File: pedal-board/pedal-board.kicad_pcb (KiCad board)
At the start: 2 copper layers, 168 x 64 mm, 42 parts, among them J1 AudioJack0, J2 AudioJack1, J3 AudioJack2, J4 AudioJack3, J5 SPI, U1 MCP3004

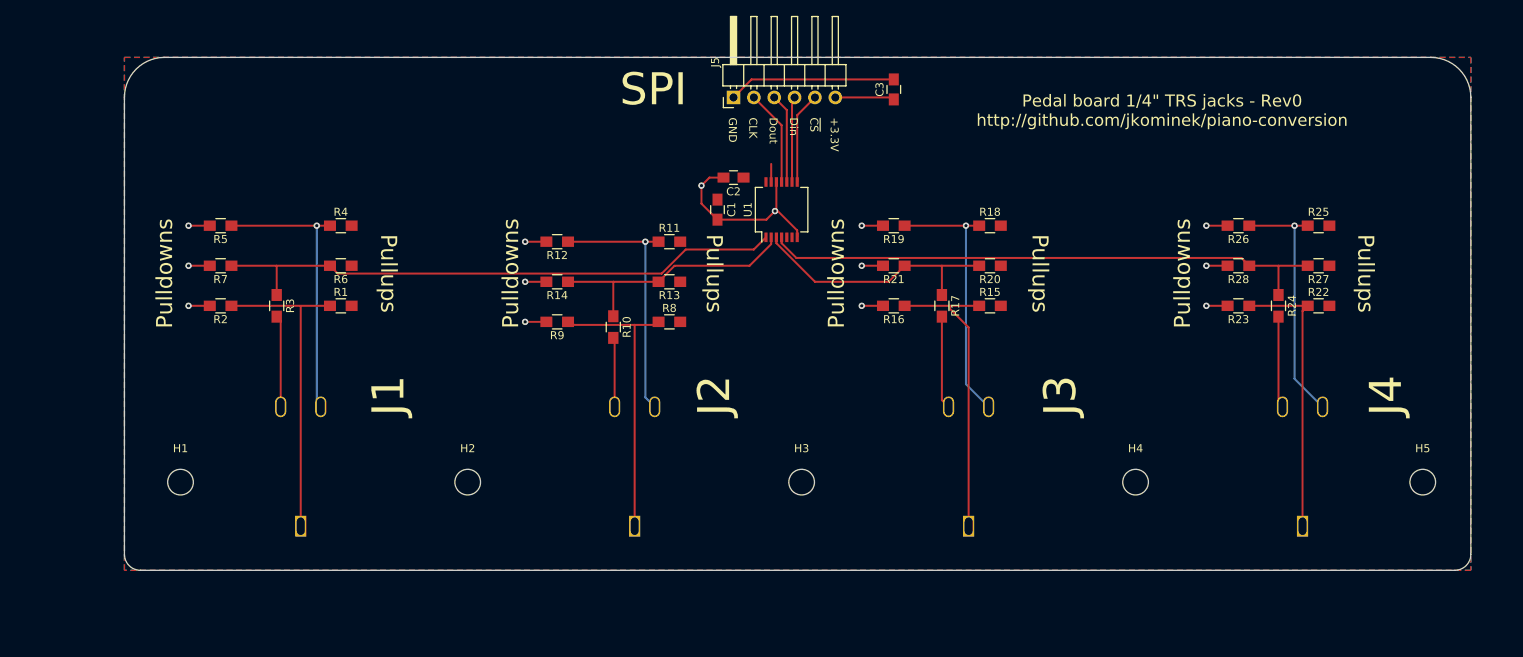
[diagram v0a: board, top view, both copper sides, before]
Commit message: Convert pedal board over to I2C/Qwiic. Adjust mounting hole spacing.
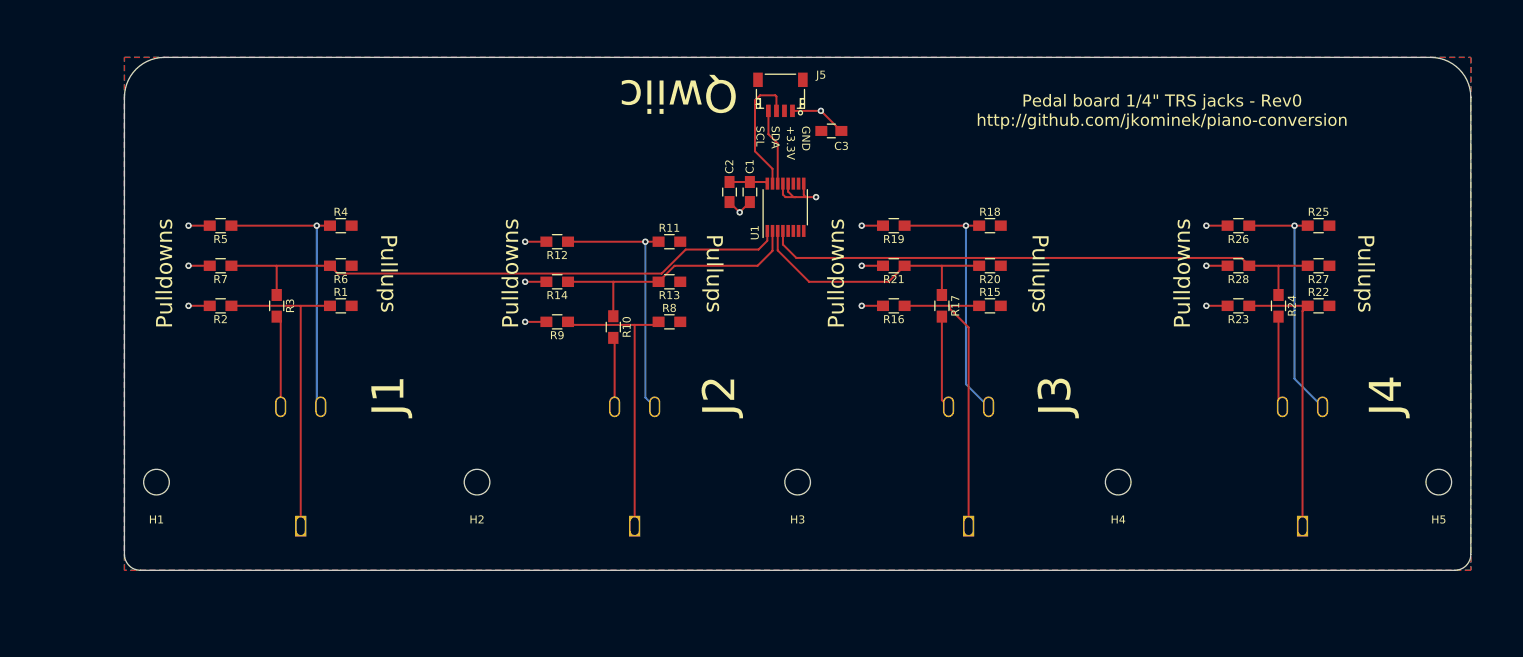
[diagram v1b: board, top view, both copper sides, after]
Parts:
- J5: value SPI -> Qwiic; footprint Pin_Headers:Pin_Header_Angled_1x06_Pitch2.54mm -> Connectors_JST:JST_SH_SM04B-SRSS-TB_04x1.00mm_Angled
- U1: value MCP3004 -> ADS7830; footprint Housings_SSOP:SSOP-14_5.3x6.2mm_Pitch0.65mm -> Housings_SSOP:TSSOP-16_4.4x5mm_Pitch0.65mm
- moved C3 9.36 mm to (116.2, 43.2), turned to 0 degrees
- moved J5 5.86 mm to (109.9, 38.7), turned to 180 degrees
- moved C1 4.60 mm to (106.0, 50.8)
- moved H1 3.00 mm to (32.0, 87.0)
- moved H4 2.17 mm to (152.0, 87.0)
- moved H5 2.00 mm to (192.0, 87.0)
- moved C2 1.87 mm to (103.5, 50.8), turned to 270 degrees
- moved H2 1.17 mm to (72.0, 87.0)
- moved U1 0.57 mm to (110.5, 52.7)
- moved H3 0.50 mm to (112.0, 87.0)
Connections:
- J5 pad 2: Net-(J5-Pad2) -> +3V3
- J5 pad 3: Net-(J5-Pad3) -> /SDA
- J5 pad 4: Net-(J5-Pad4) -> /SCL
- U1 pad 10: Net-(J5-Pad3) -> (no net)
- U1 pad 11: Net-(J5-Pad2) -> (no net)
- U1 pad 13: +3V3 -> GND
- U1 pad 14: +3V3 -> /SCL
- U1 pad 7: GND -> (no net)
- U1 pad 8: Net-(J5-Pad5) -> (no net)
- U1 pad 9: Net-(J5-Pad4) -> GND
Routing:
- net GND: track 76.8 -> 52.2 mm, vias 14 -> 15
- net /SDA: track 0.00 -> 16.1 mm
- net Net-(J5-Pad2): track 12.0 -> 0.00 mm
- net Net-(J5-Pad5): track 11.5 -> 0.00 mm
- net Net-(J5-Pad3): track 11.2 -> 0.00 mm
- net Net-(J5-Pad4): track 10.7 -> 0.00 mm
- net /SCL: track 0.00 -> 9.56 mm
- net +3V3: track 9.65 -> 4.79 mm
- net /CH1: track 32.4 -> 33.9 mm
- net /CH0: track 72.6 -> 73.8 mm
- net /CH2: track 32.5 -> 33.7 mm
- net /CH3: track 71.2 -> 71.9 mm
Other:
- board text added: "Qwiic"
- board text added: "SCL"
- board text added: "SDA"
- board text removed: "CLK"
- board text removed: "Din"
- board text removed: "Dout"
- board text removed: "SPI"
- board text removed: "~CS~"

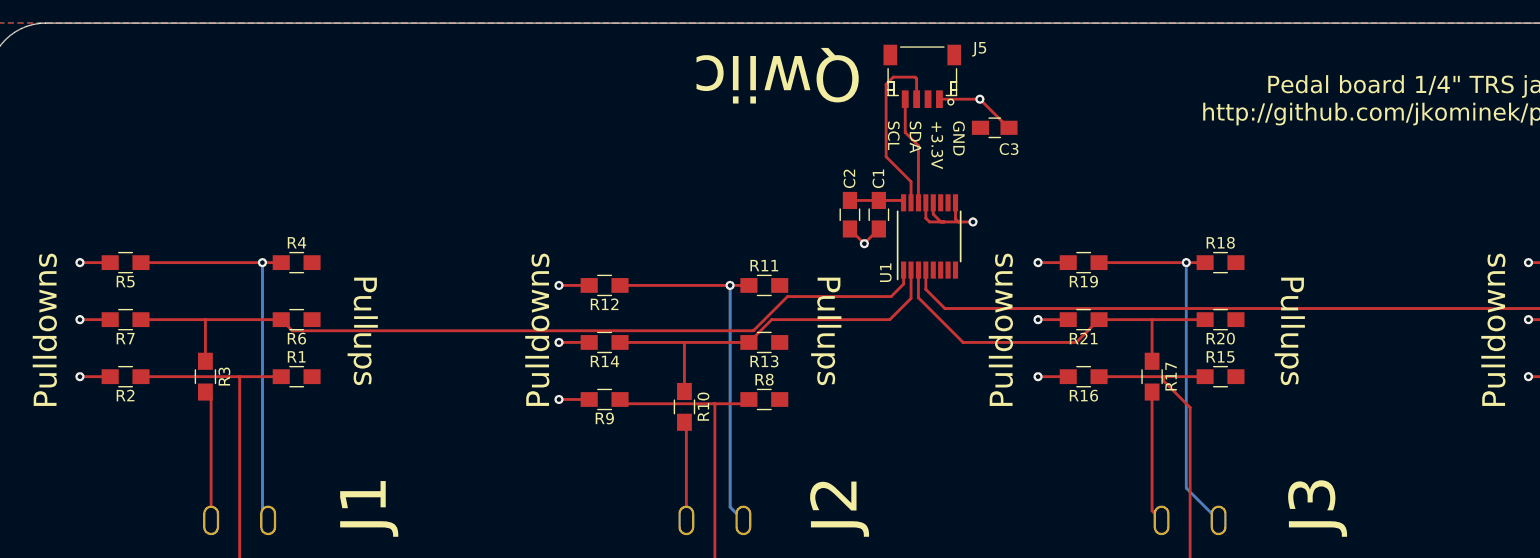
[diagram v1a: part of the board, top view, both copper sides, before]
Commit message: Complete pedal board I2C conversion; make I2C address configurable.
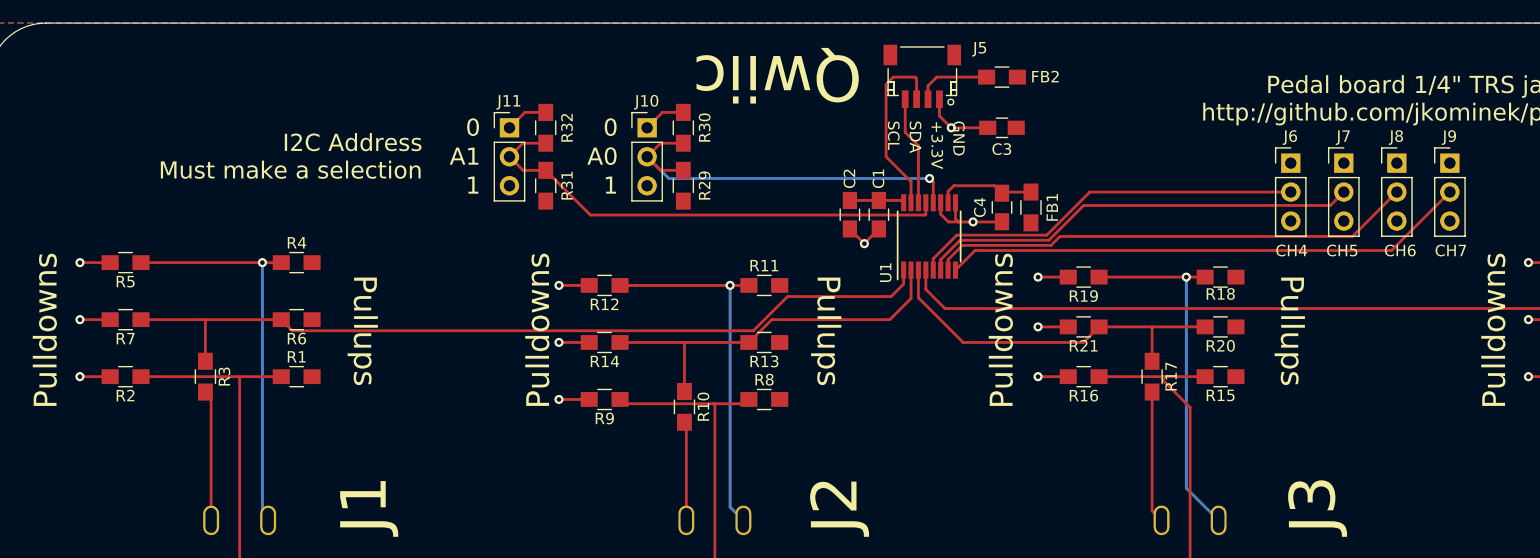
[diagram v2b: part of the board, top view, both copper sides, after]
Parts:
- added C4: 0.1uF, Capacitors_SMD:C_0805_HandSoldering, F.Cu at (116.8, 50.2)
- added FB1: FB, Inductors_SMD:L_0805_HandSoldering, F.Cu at (119.4, 50.2)
- added FB2: FB, Inductors_SMD:L_0805_HandSoldering, F.Cu at (116.8, 38.7)
- added J10: CH7, Pin_Headers:Pin_Header_Straight_1x03_Pitch2.54mm, F.Cu at (85.7, 43.2)
- added J11: CH7, Pin_Headers:Pin_Header_Straight_1x03_Pitch2.54mm, F.Cu at (73.7, 43.2)
- added J6: CH7, Pin_Headers:Pin_Header_Straight_1x03_Pitch2.54mm, F.Cu at (142.2, 46.3)
- added J7: CH7, Pin_Headers:Pin_Header_Straight_1x03_Pitch2.54mm, F.Cu at (146.8, 46.3)
- added J8: CH7, Pin_Headers:Pin_Header_Straight_1x03_Pitch2.54mm, F.Cu at (151.5, 46.3)
- added J9: CH7, Pin_Headers:Pin_Header_Straight_1x03_Pitch2.54mm, F.Cu at (156.1, 46.3)
- added R29: DNP, Resistors_SMD:R_0805_HandSoldering, F.Cu at (88.9, 48.3)
- added R30: DNP, Resistors_SMD:R_0805_HandSoldering, F.Cu at (88.9, 43.2)
- added R31: DNP, Resistors_SMD:R_0805_HandSoldering, F.Cu at (76.8, 48.3)
- added R32: DNP, Resistors_SMD:R_0805_HandSoldering, F.Cu at (76.8, 43.2)
- moved R18 1.27 mm to (136.0, 56.3)
- moved R19 1.27 mm to (124.0, 56.3)
- moved C3 0.64 mm to (116.8, 43.2), turned to 180 degrees
- moved R20 0.63 mm to (136.0, 60.6)
- moved R21 0.63 mm to (124.0, 60.6)
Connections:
- J5 pad 2: +3V3 -> Net-(FB2-Pad2)
- U1 pad 10: (no net) -> Net-(C4-Pad1)
- U1 pad 11: (no net) -> GND
- U1 pad 12: GND -> /A0
- U1 pad 13: GND -> /A1
- U1 pad 5: (no net) -> Net-(J6-Pad2)
- U1 pad 6: (no net) -> Net-(J7-Pad2)
- U1 pad 7: (no net) -> Net-(J8-Pad2)
- U1 pad 8: (no net) -> Net-(J9-Pad2)
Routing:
- net Net-(J9-Pad2): track 0.00 -> 46.2 mm
- net /A1: track 0.00 -> 43.3 mm
- net Net-(J8-Pad2): track 0.00 -> 42.7 mm
- net Net-(J7-Pad2): track 0.00 -> 38.7 mm
- net /A0: track 0.00 -> 35.2 mm, vias 0 -> 1
- net Net-(J6-Pad2): track 0.00 -> 34.8 mm
- net Net-(C4-Pad1): track 0.00 -> 8.78 mm
- net Net-(FB2-Pad2): track 0.00 -> 6.62 mm
- net GND: track 52.2 -> 57.5 mm
- net Net-(J3-PadT): track 33.1 -> 31.8 mm
- net /CH2: track 33.7 -> 32.8 mm
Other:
- board text added: "0"
- board text added: "1"
- board text added: "A0"
- board text added: "A1"
- board text added: "CH4"
- board text added: "CH5"
- board text added: "CH6"
- board text added: "CH7"
- board text added: "I2C Address Must make a selection"

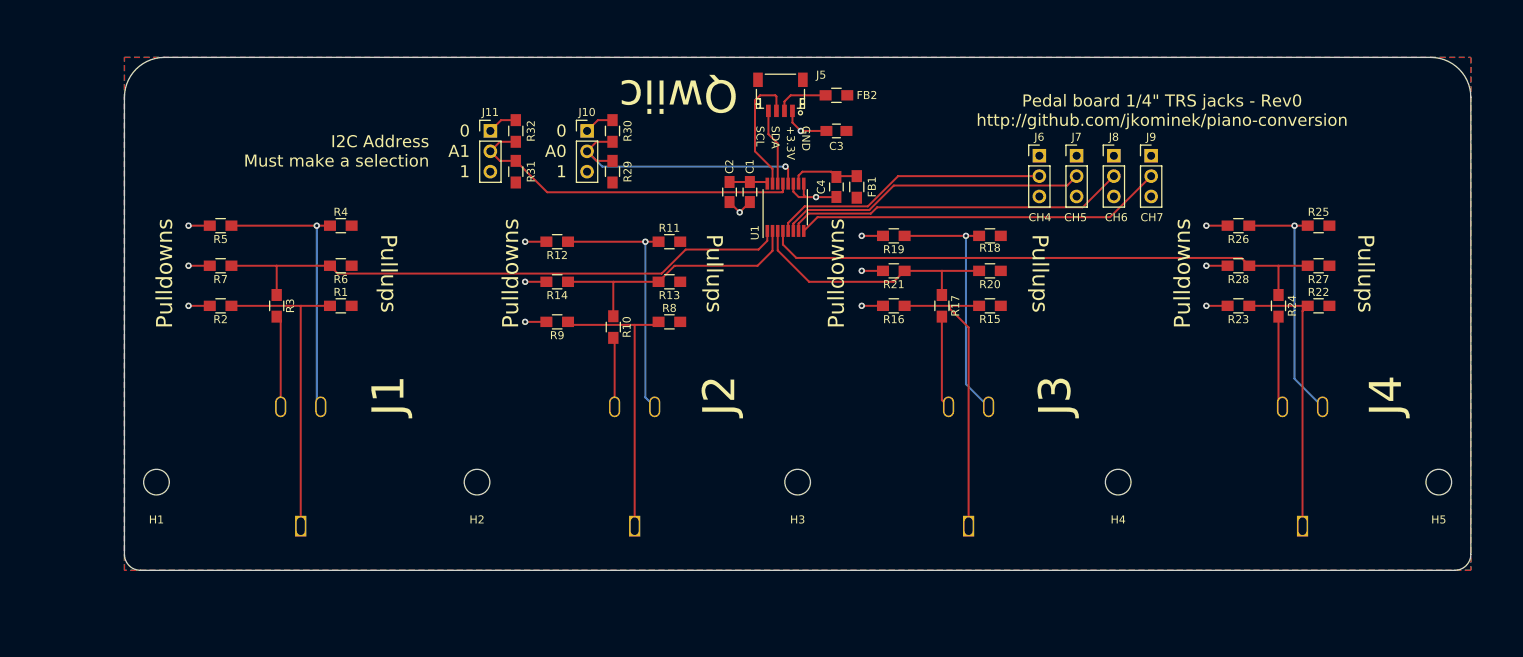
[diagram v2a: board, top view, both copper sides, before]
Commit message: Second Qwiic header, semi-split analog power rail, silkscreen tweaks.
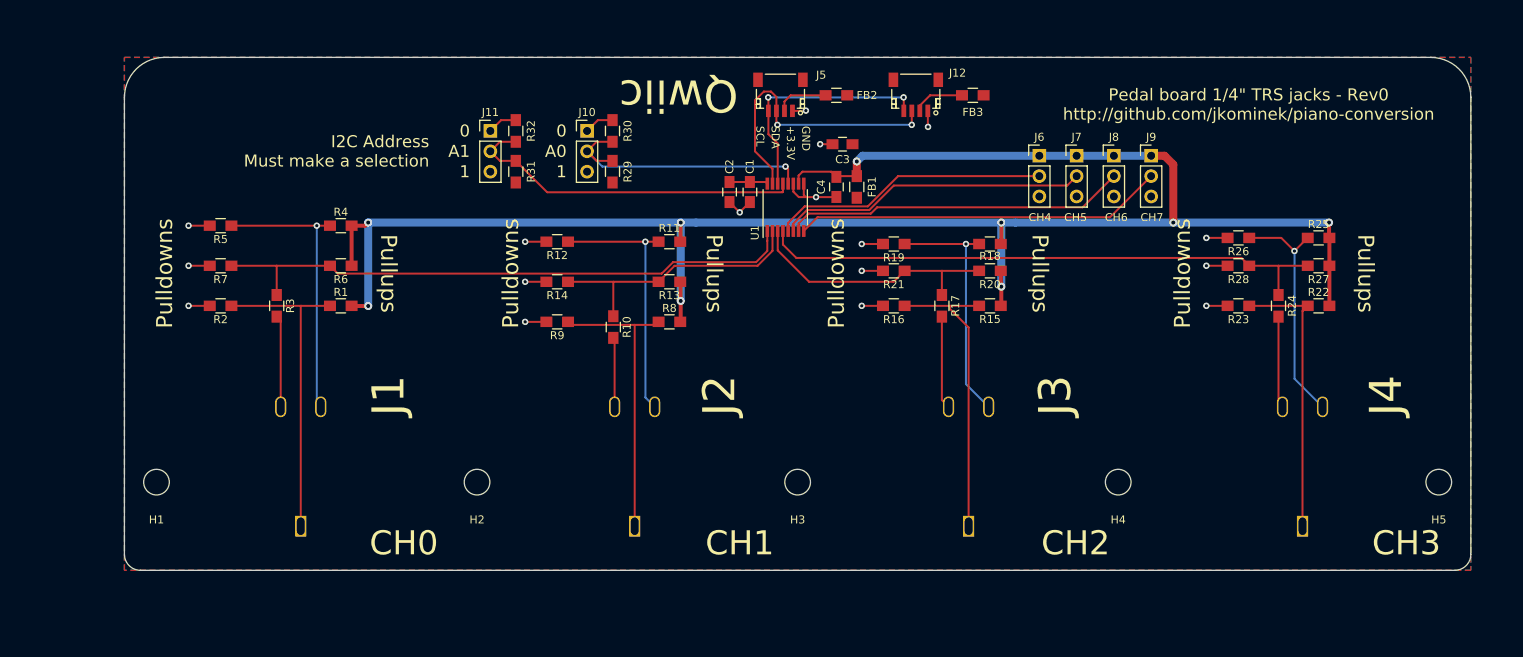
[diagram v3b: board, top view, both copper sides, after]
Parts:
- added FB3: FB, Inductors_SMD:L_0805_HandSoldering, F.Cu at (133.9, 38.7)
- added J12: Qwiic, Connectors_JST:JST_SH_SM04B-SRSS-TB_04x1.00mm_Angled, F.Cu at (126.7, 38.7)
- moved C3 1.82 mm to (117.6, 44.8)
- moved R25 1.52 mm to (177.0, 56.5)
- moved R26 1.52 mm to (167.0, 56.5)
- moved R18 1.02 mm to (136.0, 57.3)
- moved R19 1.02 mm to (124.0, 57.3)
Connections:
- C4 pad 1: Net-(C4-Pad1) -> +3.3VA
- FB1 pad 2: Net-(C4-Pad1) -> +3.3VA
- J6 pad 1: +3V3 -> +3.3VA
- J7 pad 1: +3V3 -> +3.3VA
- J8 pad 1: +3V3 -> +3.3VA
- J9 pad 1: +3V3 -> +3.3VA
- R1 pad 2: +3V3 -> +3.3VA
- R11 pad 2: +3V3 -> +3.3VA
- R13 pad 1: +3V3 -> +3.3VA
- R15 pad 2: +3V3 -> +3.3VA
- R18 pad 2: +3V3 -> +3.3VA
- R20 pad 1: +3V3 -> +3.3VA
- R22 pad 2: +3V3 -> +3.3VA
- R25 pad 2: +3V3 -> +3.3VA
- R27 pad 1: +3V3 -> +3.3VA
- R4 pad 2: +3V3 -> +3.3VA
- R6 pad 1: +3V3 -> +3.3VA
- R8 pad 2: +3V3 -> +3.3VA
- U1 pad 10: Net-(C4-Pad1) -> +3.3VA
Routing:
- net +3.3VA: track 0.00 -> 240.5 mm, vias 0 -> 9
- net /SDA: track 16.1 -> 36.7 mm, vias 0 -> 2
- net /SCL: track 9.56 -> 29.8 mm, vias 0 -> 2
- net Net-(C4-Pad1): track 8.78 -> 0.00 mm
- net Net-(FB3-Pad2): track 0.00 -> 6.45 mm
- net Net-(J4-PadT): track 31.3 -> 29.5 mm
- net Net-(J3-PadT): track 31.8 -> 30.8 mm
- net GND: track 57.5 -> 56.6 mm, vias 15 -> 17
- net /CH0: track 73.8 -> 74.6 mm
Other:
- board text added: "CH0"
- board text added: "CH1"
- board text added: "CH2"
- board text added: "CH3"
